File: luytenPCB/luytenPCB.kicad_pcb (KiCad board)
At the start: 2 copper layers, 80.9 x 35.6 mm, 39 parts, among them IC1 DRV8212DRLR, IC2 DRV8212DRLR, J1 Battery, J10 START_M, J11 DIST_C, J2 BDC1, J3 BDC2, J4 LINE_RF, J5 LINE_LF, J6 DIST_L, J7 DIST_LM, J8 DIST_R, J9 DIST_RM, SW1 SW_SPST, SW2 ProgSelect

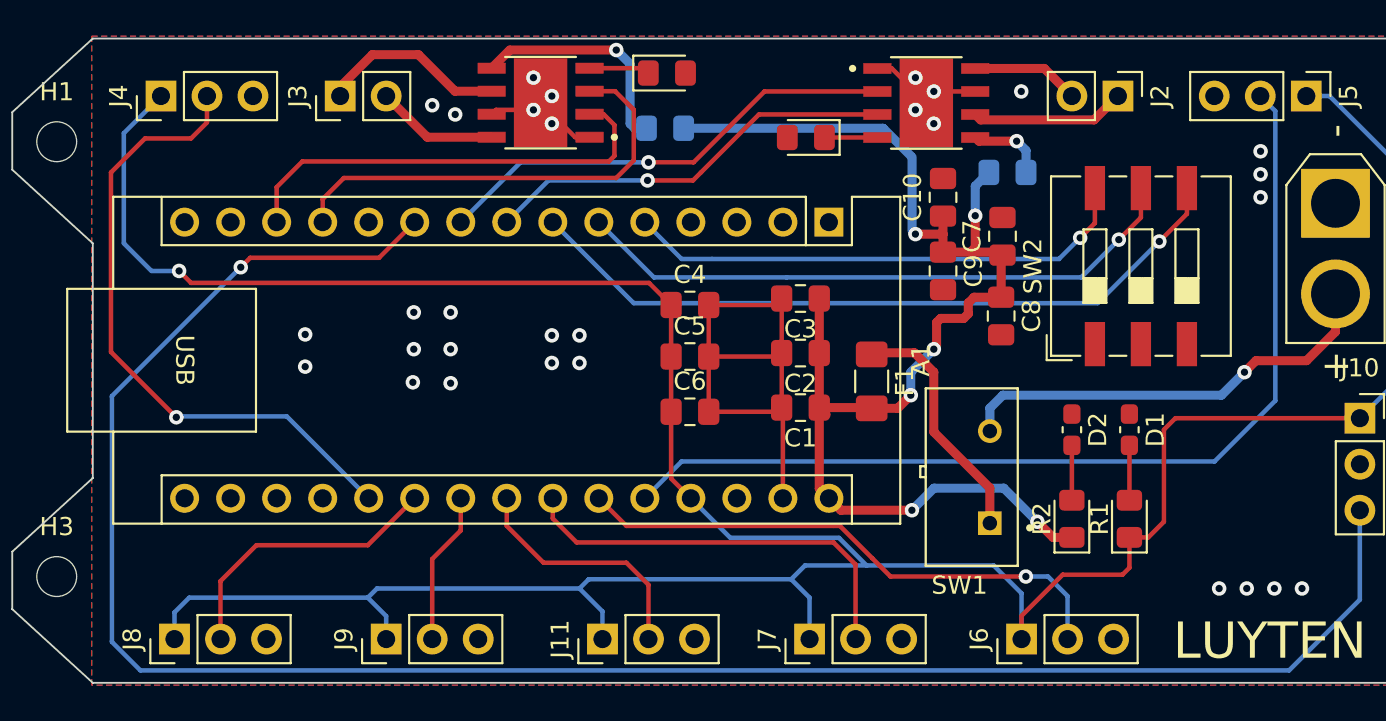
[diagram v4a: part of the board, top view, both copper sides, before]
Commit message: updated motor driver drv8212
changed some connections for compatibility with digital and analog dist sensors, updated optional kill switch circuit break
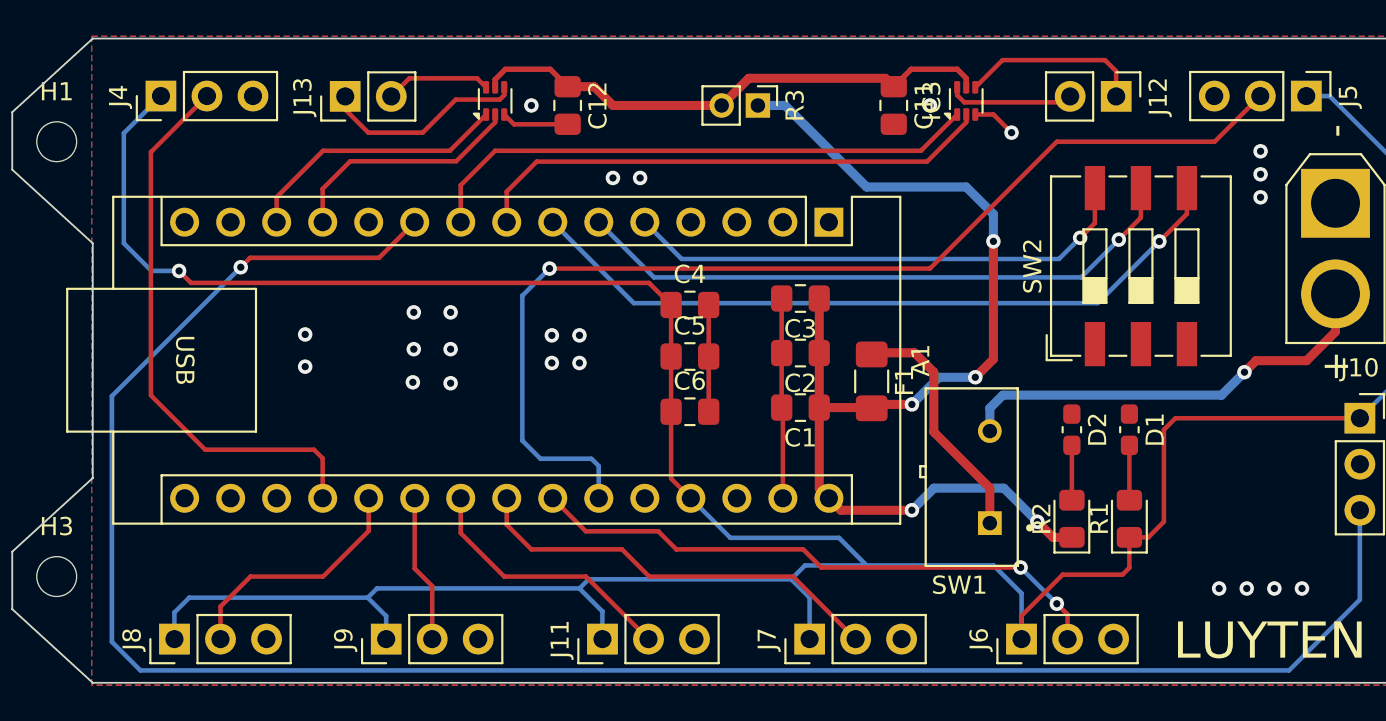
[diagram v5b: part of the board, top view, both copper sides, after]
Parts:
- removed C10, C9: 47uF, Capacitor_SMD:C_0805_2012Metric_Pad1.18x1.45mm_HandSolder
- removed C7, C8: 0.1uF, Capacitor_SMD:C_0805_2012Metric_Pad1.18x1.45mm_HandSolder
- removed IC1, IC2: DRV8212DRLR, DRV8871DDAR:VREG_LM5017MR_NOPB
- removed J2: BDC1, Connector_PinHeader_2.54mm:PinHeader_1x02_P2.54mm_Vertical
- removed J3: BDC2, Connector_PinHeader_2.54mm:PinHeader_1x02_P2.54mm_Vertical
- removed R4: 600, Diode_SMD:D_0805_2012Metric_Pad1.15x1.40mm_HandSolder
- removed R8, R9: 30k, Diode_SMD:D_0805_2012Metric_Pad1.15x1.40mm_HandSolder
- added C11: 0.1uF, Capacitor_SMD:C_0805_2012Metric_Pad1.18x1.45mm_HandSolder, F.Cu at (90.5, 31.0)
- added C12: 0.1uF, Capacitor_SMD:C_0805_2012Metric_Pad1.18x1.45mm_HandSolder, F.Cu at (72.5, 31.0)
- added IC3: DRV8212DRLR, Package_TO_SOT_SMD:SOT-563, F.Cu at (94.5, 30.8)
- added IC4: DRV8212DRLR, Package_TO_SOT_SMD:SOT-563, F.Cu at (68.5, 30.8)
- added J12: BDC1, Connector_PinHeader_2.54mm:PinHeader_1x02_P2.54mm_Vertical, F.Cu at (102.8, 30.5)
- added J13: BDC2, Connector_PinHeader_2.54mm:PinHeader_1x02_P2.54mm_Vertical, F.Cu at (60.2, 30.5)
- R3: value 600 -> 0; footprint Diode_SMD:D_0805_2012Metric_Pad1.15x1.40mm_HandSolder -> Connector_PinHeader_2.00mm:PinHeader_1x02_P2.00mm_Vertical; moved to F.Cu
- moved R3 14.3 mm to (83.0, 31.0), turned to -90 degrees
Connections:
- A1 pad 12: MDC2_1 -> MDC2_2
- A1 pad 13: MDC2_2 -> MDC2_1
- A1 pad 19: unconnected-(A1-A0-Pad19) -> RF_INT
- A1 pad 20: RF_INT -> DIST_R_INT
- A1 pad 21: DIST_R_INT -> DIST_RM_INT
- A1 pad 22: DIST_RM_INT -> DIST_C_INT
- A1 pad 23: DIST_C_INT -> DIST_LM_INT
- A1 pad 24: DIST_LM_INT -> DIST_L_INT
- A1 pad 25: DIST_L_INT -> LF_INT
- A1 pad 26: LF_INT -> unconnected-(A1-A7-Pad26)
- A1 pad 8: MDC1_1 -> MDC1_2
- A1 pad 9: MDC1_2 -> MDC1_1
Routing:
- net Net-(IC3-VM): track 4.31 -> 29.4 mm, vias 1 -> 0
- net GND: track 41.7 -> 24.2 mm, vias 30 -> 24
- net Net-(IC2-VM): track 12.7 -> 0.00 mm, vias 1 -> 0
- net ArduinoVIN: track 73.1 -> 60.8 mm, vias 6 -> 5
- net Net-(IC4-OUT2): track 0.00 -> 11.3 mm
- net MDC2_2: track 24.6 -> 13.3 mm
- net Net-(IC2-OUT1): track 10.4 -> 0.00 mm
- net MDC2_1: track 25.0 -> 14.8 mm
- net Net-(IC3-OUT2): track 0.00 -> 10.0 mm
- net Net-(IC1-OUT1): track 8.54 -> 0.00 mm
- net MDC1_1: track 22.9 -> 31.1 mm, vias 1 -> 0
- net Net-(IC3-OUT1): track 0.00 -> 6.96 mm
- net Net-(IC2-OUT2): track 6.76 -> 0.00 mm
- net Net-(IC1-OUT2): track 5.97 -> 0.00 mm
- net Net-(IC4-OUT1): track 0.00 -> 5.86 mm
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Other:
- board text added: "Luyten_MiniSumo_v3.1 - Alex Peng '24"
- board text removed: "Luyten_MiniSumo_v1 - Alex Peng '24"
